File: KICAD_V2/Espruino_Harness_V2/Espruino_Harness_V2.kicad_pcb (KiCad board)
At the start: 2 copper layers, 7 parts, among them U1 Espruino-MDBT42Q-Breakout, U2 Espruino-Pico-1v4, U3 Raspberry-Pi-Pico-Family, U4 ESP32-S3-DevKitC-1, U5 OLIMEX-ESP32-S3-DevKit-LiPo-EA, U6 ESP32-DevKitC-V4, U7 ESP32-C3-DevKitC-02

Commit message: Add V2 routing logic library prototypes
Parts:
- removed U3: Raspberry-Pi-Pico-Family, V2_Targets:Raspberry-Pi-Pico-Family-Wirewrap
- added R4: 470R, V2_Harness:R_Axial_DIN0204_L3.6mm_D1.6mm_P2.54mm_Vertical, F.Cu at (149.9, 45.7)
- added SEL_D26: LOOP_B / DS2413_PIOB, V2_Harness:PinHeader_1x03_P2.54mm_Vertical, F.Cu at (146.0, 42.2)
- added U8: TMUX1204DGSR, V2_Harness:DGS0010A-IPC_B, F.Cu at (168.1, 42.0)

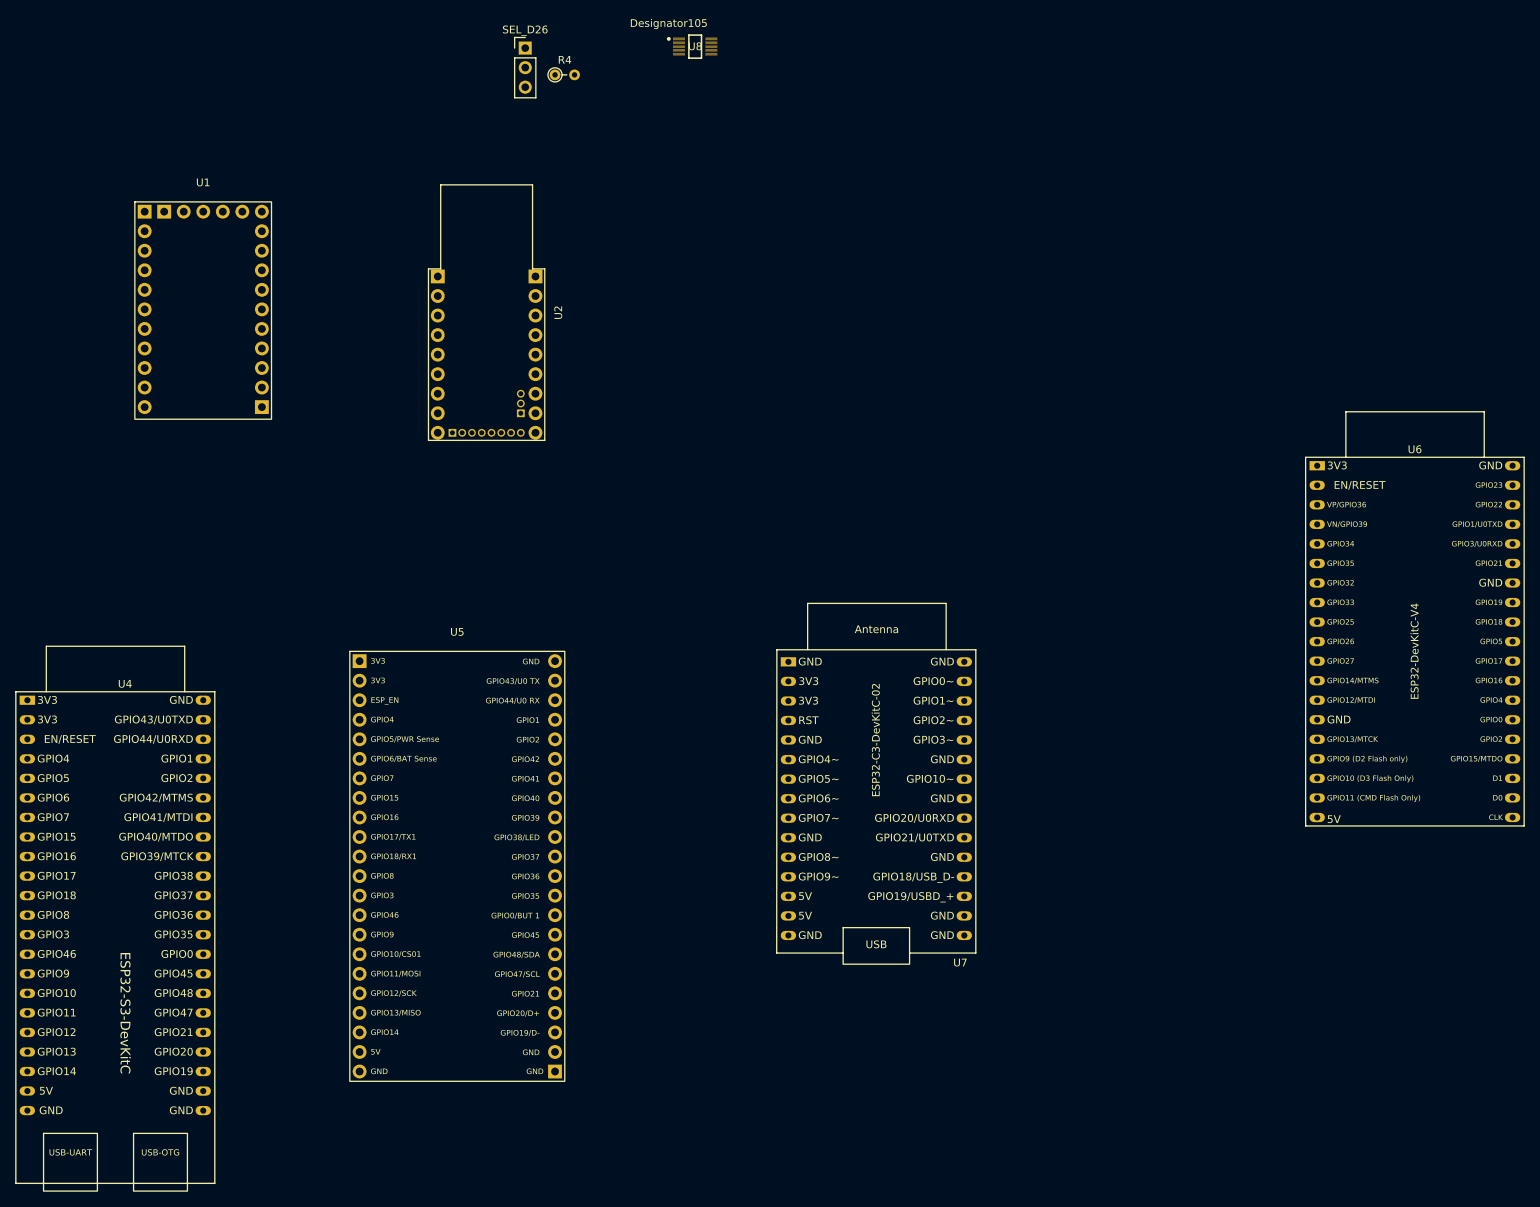
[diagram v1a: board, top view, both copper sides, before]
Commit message: Add Espruino Pico castellated footprints
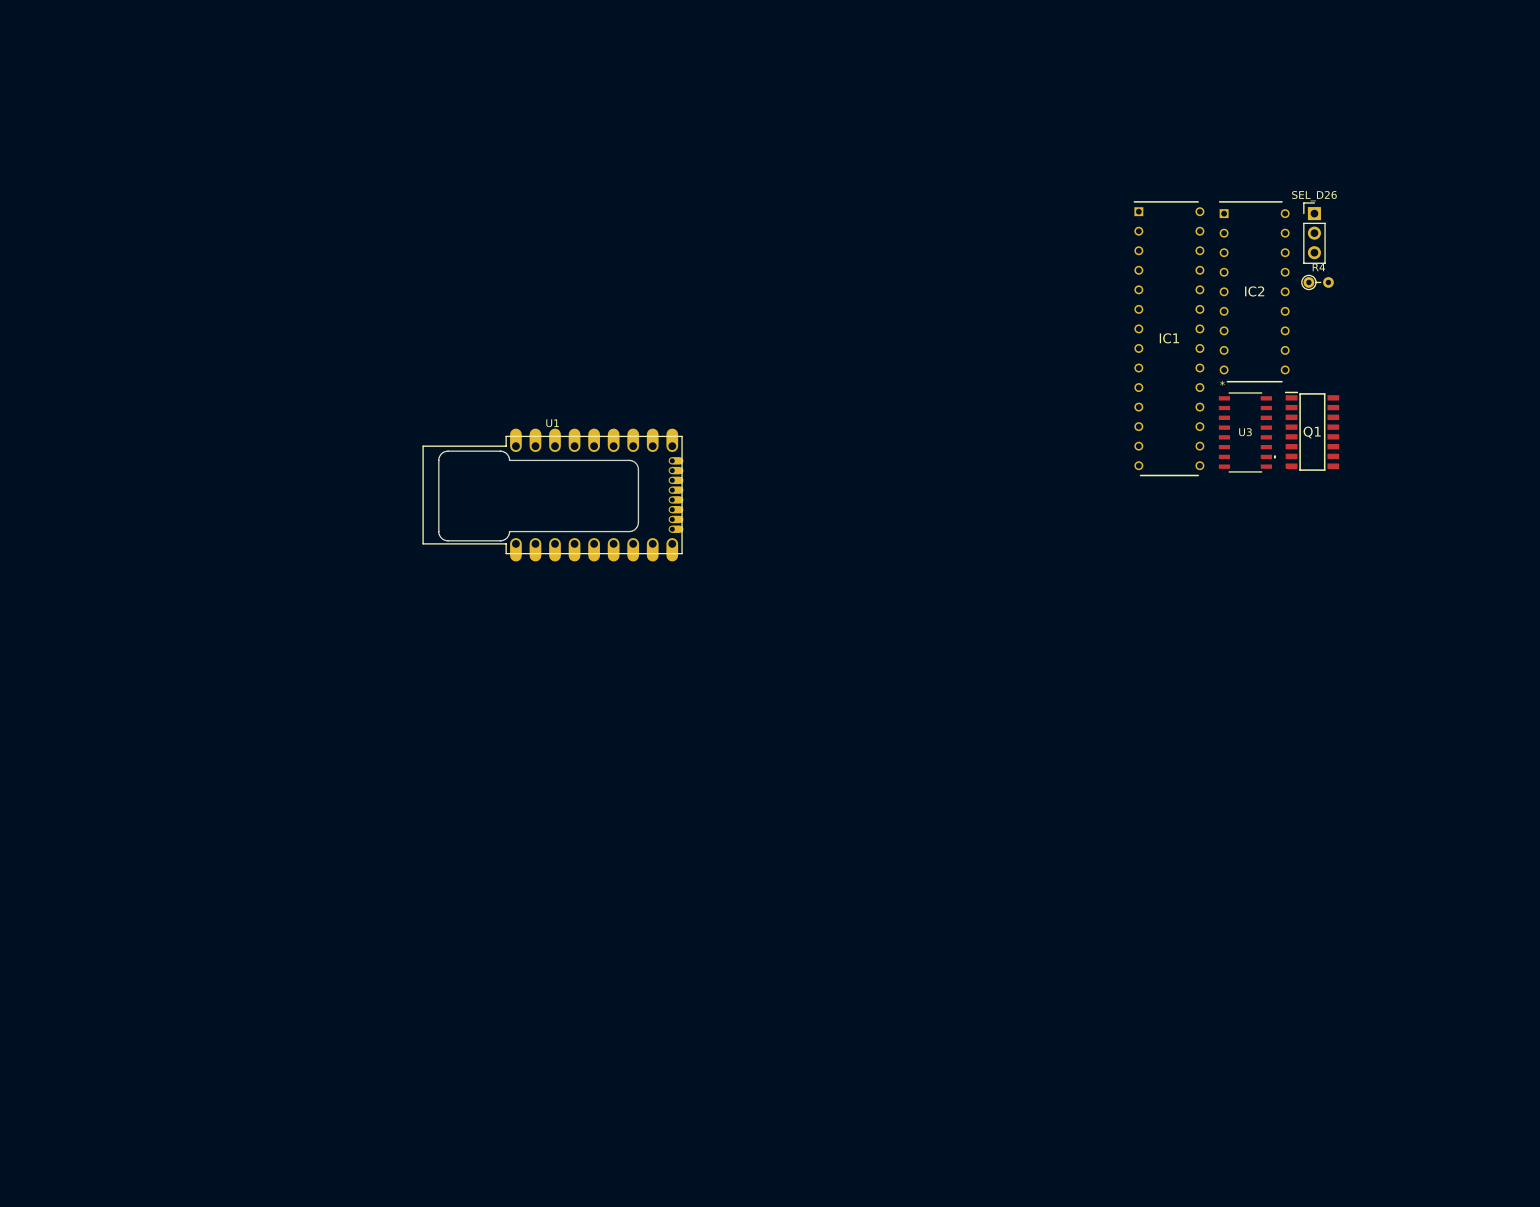
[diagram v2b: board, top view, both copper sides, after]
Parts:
- removed U2: Espruino-Pico-1v4, V2_Targets:Espruino-Pico-1v4-Wirewrap
- removed U4: ESP32-S3-DevKitC-1, V2_Targets:ESP32-S3-DevKitC-1
- removed U5: OLIMEX-ESP32-S3-DevKit-LiPo-EA, V2_Targets:OLIMEX-ESP32-S3-DevKit-LiPo-EA-Wirewrap
- removed U6: ESP32-DevKitC-V4, V2_Targets:ESP32-DevKitC-V4-Wirewrap
- removed U7: ESP32-C3-DevKitC-02, V2_Targets:ESP32-C3-DevKitC-02
- removed U8: TMUX1204DGSR, V2_Harness:DGS0010A-IPC_B
- added IC1: MCP23017-E_SP, SamacSys_Parts:DIP794W56P254L3486H508Q28N, F.Cu at (229.7, 80.0)
- added IC2: MCP23008-E_P, SamacSys_Parts:DIP794W56P254L2286H533Q18N, F.Cu at (240.8, 73.9)
- added Q1: DG409LEDY-GE3, SamacSys_Parts:SOIC127P600X175-16N, F.Cu at (248.3, 92.1)
- added U3: TMUX1204DGSR, V2_Harness:SOIC_EDY-GE3_VIS, F.Cu at (239.6, 92.2)
- U1: value Espruino-MDBT42Q-Breakout -> Espruino-Pico-1v4; footprint V2_Targets:Espruino-MDBT42Q-Breakout-Wirewrap -> V2_Targets:Espruino-Pico-1v4-Gordon-Shim
- moved SEL_D26 104.8 mm to (248.6, 63.8)
- moved R4 101.6 mm to (247.8, 72.7)
- moved U1 74.1 mm to (158.8, 100.3)
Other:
- board outline added: 25.9 x 11.7 mm
- board text removed: "Dimensions: 18mm x 28mm x 4mm thick"
- board text removed: "Raspberry-Pi-Pico-Family"
